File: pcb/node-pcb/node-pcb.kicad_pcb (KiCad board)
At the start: 4 copper layers, 44 x 44 mm, 53 parts, among them J1 TYPE-C-31-M-12, J2 BM08B-GHS-TBT(LF)(SN), J3 BM08B-GHS-TBT(LF)(SN), J4 TC2030, J5 AFC11-S12ICA-00, Q1 S8050, SW1 TS-1187A-B-A-B, U1 AP2112K-3.3, U2 W25Q32JVSSIQ, U3 RP2040, U4 THVD1450DR, Y1 ABM8-272-T3

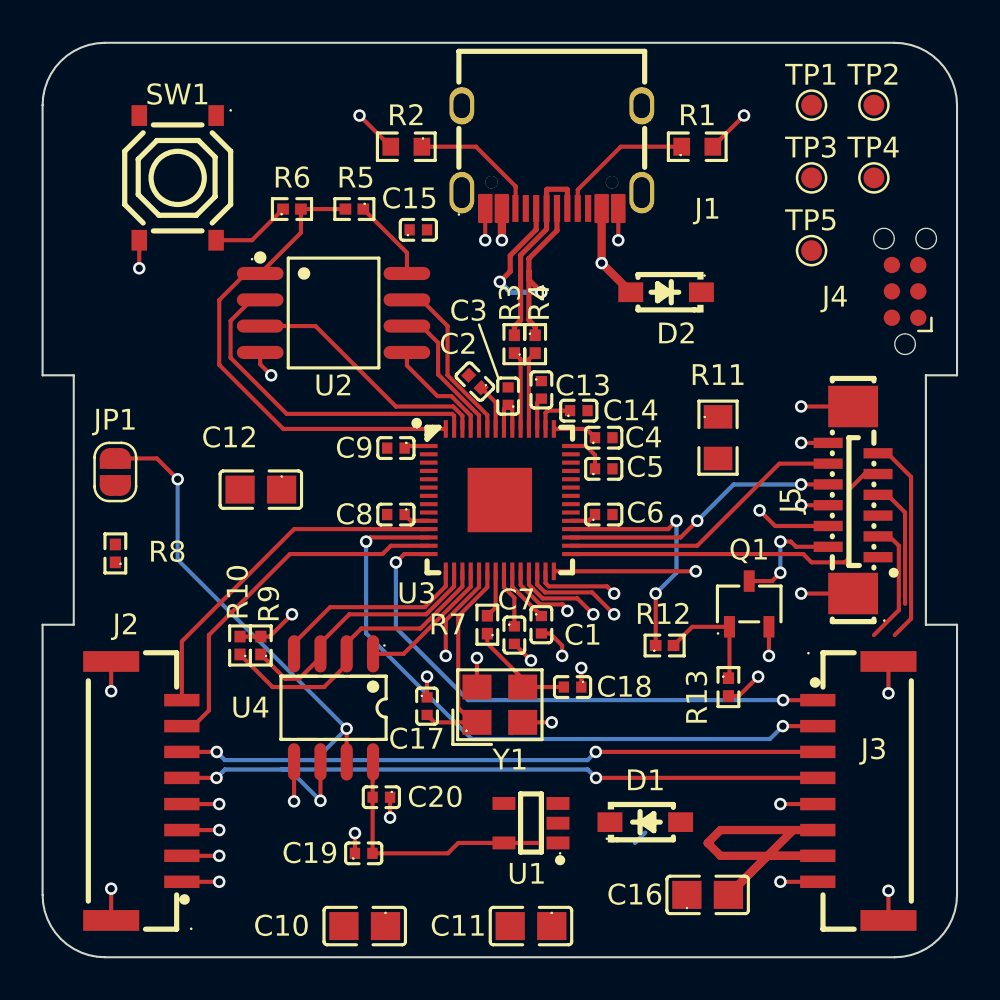
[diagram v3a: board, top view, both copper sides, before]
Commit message: Update schematic PDF with latest design revisions
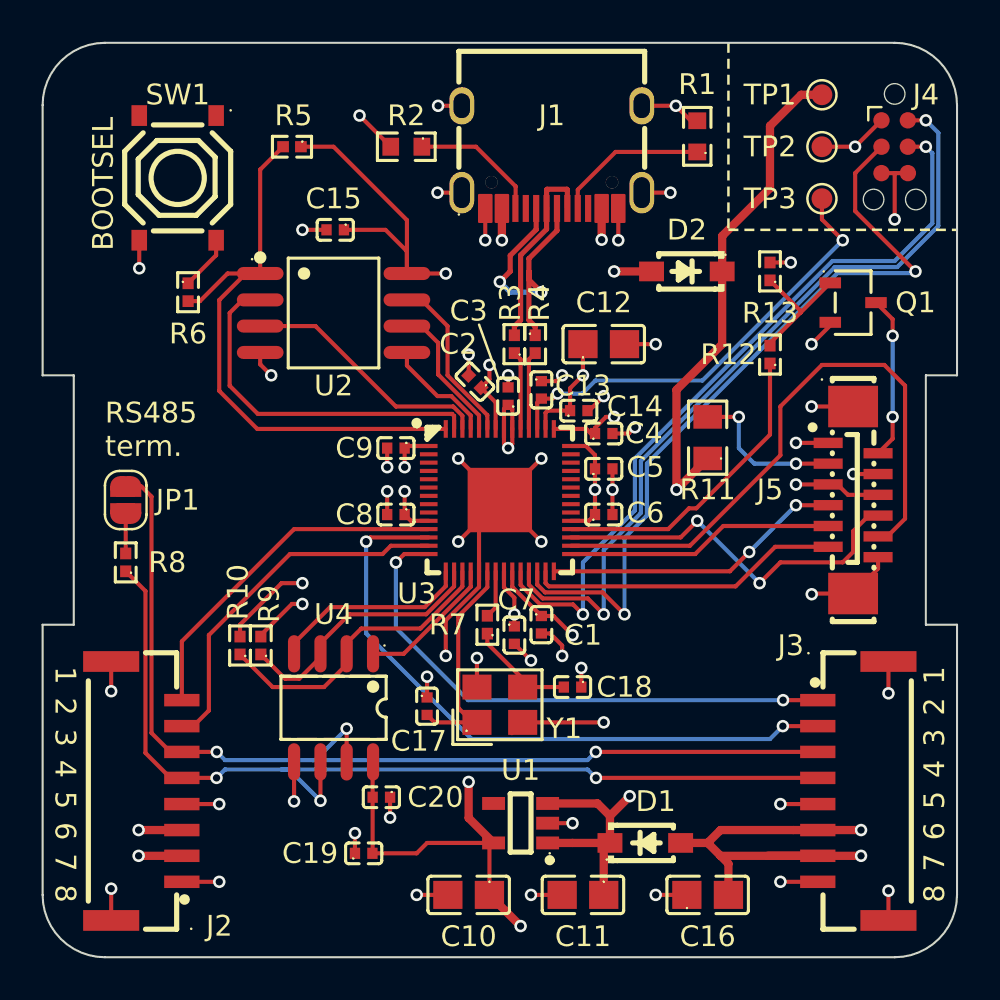
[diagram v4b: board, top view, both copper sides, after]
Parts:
- removed TP4: TP_A, TestPoint:TestPoint_Pad_D1.0mm
- removed TP5: TP_B, TestPoint:TestPoint_Pad_D1.0mm
- moved R13 20.1 mm to (113.0, 89.0), turned to 90 degrees
- moved C12 17.9 mm to (105.0, 92.5), turned to 0 degrees
- moved Q1 15.3 mm to (117.0, 90.5), turned to 180 degrees
- moved R12 14.9 mm to (113.0, 93.0), turned to 90 degrees
- moved J4 6.98 mm to (119.0, 83.0), turned to -90 degrees
- moved R6 6.40 mm to (85.0, 90.0), turned to -90 degrees
- moved C10 5.22 mm to (98.5, 119.0)
- moved R5 4.24 mm to (90.0, 83.0)
- moved C15 4.00 mm to (92.1, 87.0), turned to 180 degrees
- moved TP2 3.20 mm to (115.5, 83.0)
- moved C11 2.92 mm to (104.0, 119.0)
- moved JP1 1.44 mm to (82.0, 100.0)
- moved D2 1.41 mm to (109.0, 89.0)
- moved TP3 1.12 mm to (115.5, 85.5)
- moved D1 1.00 mm to (107.0, 116.5)
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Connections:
- C11 pad 1: /5V_LOCAL -> 5V_LOCAL
- C16 pad 2: VBUS +5V -> +5V_BUS
- D1 pad 1: /5V_LOCAL -> 5V_LOCAL
- D1 pad 2: VBUS +5V -> +5V_BUS
- D2 pad 1: /5V_LOCAL -> 5V_LOCAL
- J1 pad 1: (no net) -> GND
- J1 pad 2: (no net) -> GND
- J1 pad 3: (no net) -> GND
- J1 pad 4: (no net) -> GND
- J1 pad A1B12: (no net) -> GND
- J1 pad A4B9: (no net) -> /VBUS_USB-C
- J1 pad B1A12: (no net) -> GND
- J1 pad B4A9: (no net) -> /VBUS_USB-C
- J2 pad 2: VBUS +5V -> +5V_BUS
- J2 pad 3: VBUS +5V -> +5V_BUS
- J3 pad 6: VBUS +5V -> +5V_BUS
- J3 pad 7: VBUS +5V -> +5V_BUS
- R11 pad 1: VBUS +5V -> 5V_LOCAL
- TP1 pad 1: /5V_LOCAL -> 5V_LOCAL
- U1 pad 1: /5V_LOCAL -> 5V_LOCAL
- U1 pad 3: /5V_LOCAL -> 5V_LOCAL
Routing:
- net 5V_LOCAL: track 0.00 -> 51.8 mm, vias 0 -> 2
- net GND: track 53.8 -> 104.3 mm, vias 31 -> 54
- net +1V1: track 6.55 -> 46.8 mm, vias 0 -> 4
- net /SWDIO: track 4.34 -> 38.1 mm, vias 1 -> 2
- net /SWCLK: track 3.47 -> 36.5 mm, vias 1 -> 2
- net /RUN: track 4.93 -> 37.6 mm, vias 1 -> 2
- net +3V3: track 35.5 -> 65.0 mm, vias 1 -> 12
- net +5V_BUS: track 0.00 -> 25.2 mm, vias 0 -> 4
- net VBUS +5V: track 24.2 -> 0.00 mm, vias 2 -> 0
- net /SPI0_TX (MOSI): track 14.0 -> 29.5 mm
- net /RS485_P: track 35.3 -> 46.7 mm
- net /VBUS_USB-C: track 11.4 -> 4.84 mm, vias 2 -> 3
- net /SPI0_SCK (SCL): track 18.6 -> 12.9 mm
- net /QSPI_SS: track 23.9 -> 29.1 mm
- net /CS: track 13.4 -> 18.3 mm
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- added copper zone on In2.Cu, net +3V3
- added copper zone on In2.Cu, net +5V_BUS
- added copper zone on In2.Cu, net /VBUS_USB-C
- removed copper zone on In2.Cu, net VBUS +5V
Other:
- board text added: "1"
- board text added: "2"
- board text added: "3"
- board text added: "4"
- board text added: "5"
- board text added: "6"
- board text added: "7"
- board text added: "8"
- board text added: "BOOTSEL"
- board text added: "RS485 term."

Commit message: Refactor BOM CSV for component grouping and update part references
- Consolidated multiple entries for ceramic capacitors into grouped lines for better readability and management.
- Updated the header of the BOM CSV to reflect changes in part categorization.
- Added new entries for components with extended and basic classifications.
- Introduced a lock file for KiCad project to track user session.
- Updated schematic PDF to reflect recent changes in the design.
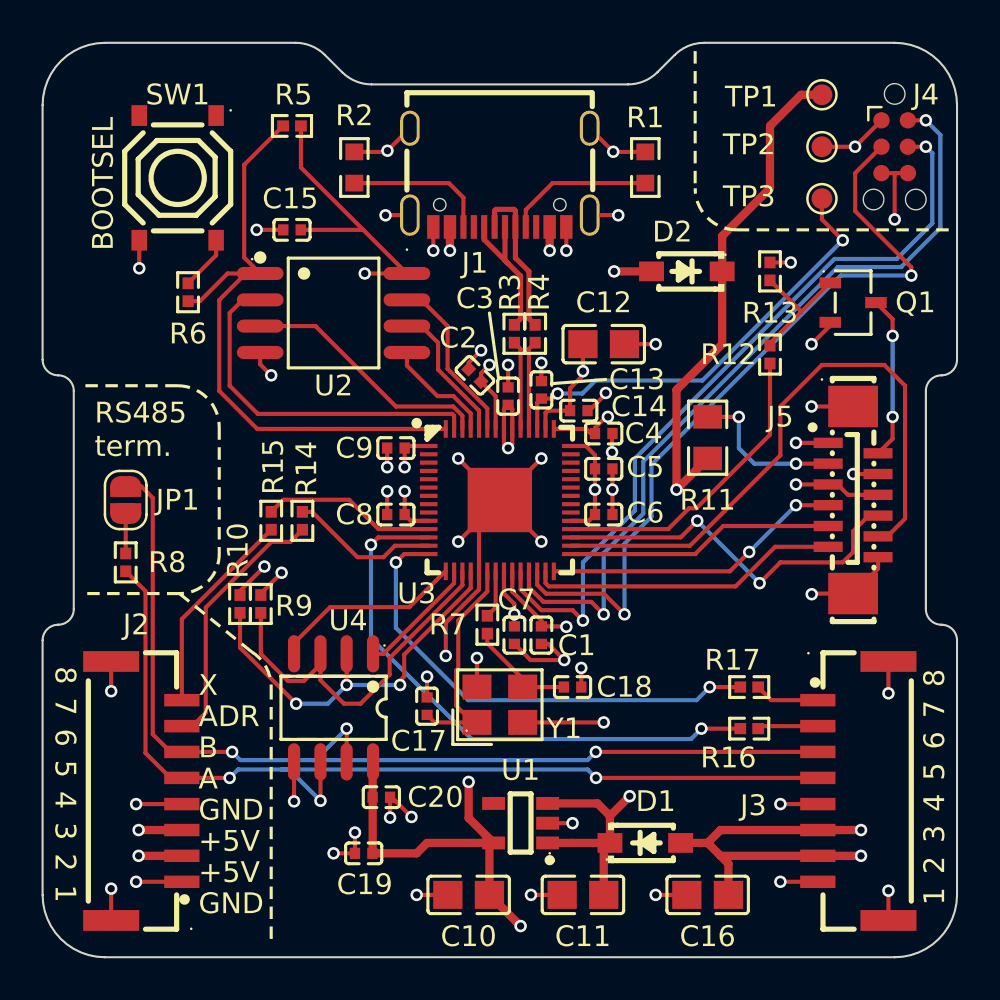
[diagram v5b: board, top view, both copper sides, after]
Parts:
- added R14: 1k, JLCPCB:R0402, F.Cu at (90.5, 101.0)
- added R15: 1k, JLCPCB:R0402, F.Cu at (89.0, 101.0)
- added R16: 1k, JLCPCB:R0402, F.Cu at (112.0, 111.0)
- added R17: 1k, JLCPCB:R0402, F.Cu at (112.0, 109.0)
- moved J1 4.30 mm to (100.0, 80.0)
- moved R1 2.92 mm to (107.0, 84.0)
- moved R2 2.69 mm to (93.0, 84.0), turned to 90 degrees
- moved C15 2.08 mm to (90.0, 87.0)
- moved R10 2.00 mm to (87.5, 105.0)
- moved R9 2.00 mm to (88.5, 105.0)
- moved R5 1.00 mm to (90.0, 82.0)
- moved C1 0.50 mm to (102.0, 106.5)
- moved R3 0.50 mm to (100.7, 92.0)
- moved R4 0.50 mm to (101.7, 92.0)
- moved C2 0.30 mm to (98.8, 94.0)
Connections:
- J1 pad A6: /USB_D- -> /USB_D+
- J1 pad A7: /USB_D+ -> /USB_D-
- J1 pad B6: /USB_D- -> /USB_D+
- J1 pad B7: /USB_D+ -> /USB_D-
- J2 pad 7: /ADDR_OUT -> Net-(J2-Pad7)
- J2 pad 8: /SPARE_OUT -> Net-(J2-Pad8)
- J3 pad 1: /SPARE_IN -> Net-(J3-Pad1)
- J3 pad 2: /ADDR_IN -> Net-(J3-Pad2)
- R10 pad 1: /GPIO14_RE -> /GPIO15_RE
- R9 pad 1: /GPIO13_DE -> /GPIO14_DE
- U3 pad 16: /GPIO13_DE -> /GPIO13_RX
- U3 pad 17: /GPIO14_RE -> /GPIO14_DE
- U3 pad 18: /GPIO15_RX -> /GPIO15_RE
- U4 pad 1: /GPIO15_RX -> /GPIO13_RX
- U4 pad 2: /GPIO14_RE -> /GPIO15_RE
- U4 pad 3: /GPIO13_DE -> /GPIO14_DE
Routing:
- net /GPIO15_RE: track 0.00 -> 19.3 mm, vias 0 -> 3
- net /GPIO14_DE: track 0.00 -> 18.3 mm
- net /GPIO14_RE: track 14.7 -> 0.00 mm
- net /GPIO13_DE: track 12.8 -> 0.00 mm
- net Net-(J2-Pad7): track 0.00 -> 12.7 mm
- net /ADDR_OUT: track 17.6 -> 7.21 mm
- net Net-(J2-Pad8): track 0.00 -> 9.98 mm
- net /SPARE_OUT: track 16.9 -> 8.41 mm
- net /USB_D-: track 14.5 -> 7.71 mm, vias 2 -> 0
- net /GPIO15_RX: track 6.78 -> 0.00 mm
- net /GPIO13_RX: track 0.00 -> 5.88 mm
- net /ADDR_IN: track 31.6 -> 27.4 mm
- net /SPARE_IN: track 26.6 -> 23.2 mm
- net Net-(J3-Pad1): track 0.00 -> 3.13 mm
- net Net-(J3-Pad2): track 0.00 -> 2.92 mm
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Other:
- outline, holes or cut-outs redrawn
- board text added: "+5V"
- board text added: "A"
- board text added: "ADR"
- board text added: "B"
- board text added: "GND"
- board text added: "X"
